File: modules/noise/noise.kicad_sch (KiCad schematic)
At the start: 25 parts, among them U1 ATtiny1616-M, U2 MCP6002-xSN, U3 MCP6002-xSN

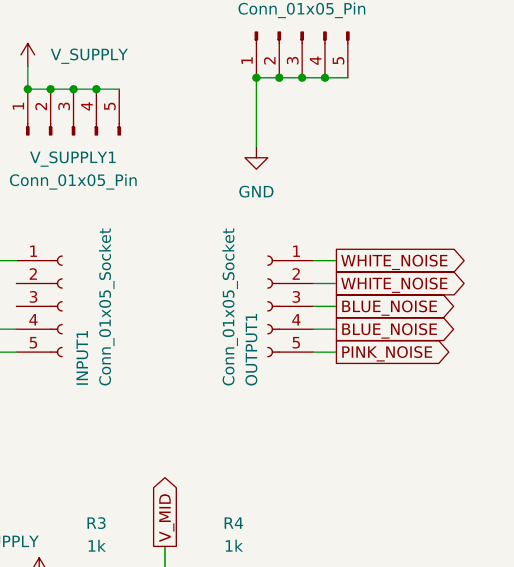
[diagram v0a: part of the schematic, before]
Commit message: noise: add MIDI Thru support
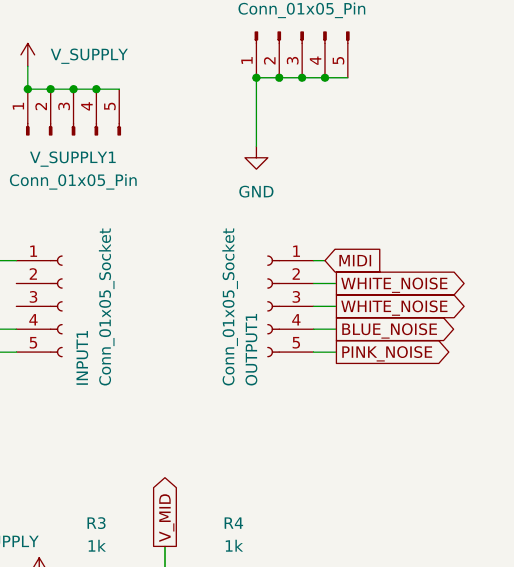
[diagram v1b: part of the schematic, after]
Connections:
- net BLUE_NOISE: no longer OUTPUT1.3 (Pin_3)
- net MIDI: now also OUTPUT1.1 (Pin_1)
- net WHITE_NOISE: now also OUTPUT1.3 (Pin_3); no longer OUTPUT1.1 (Pin_1)
